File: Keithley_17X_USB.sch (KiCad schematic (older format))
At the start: 17 parts

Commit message: added more stuff!
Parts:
- removed U?: TLP281-4, Package_SO:SOIC-16_4.55x10.3mm_P1.27mm, symbol Isolator:TLP291-4
- added C?: 100nF, symbol Device:C
- added C? (x3): 1uF, symbol Device:C
- added RN? (x2): 10k, symbol Device:R_Pack04
- added U? (x2): TLP281-4, Package_SO:SOIC-16_4.55x10.3mm_P1.27mm, symbol TLP291-4:TLP281-4
- added U?: TPS782, symbol TPS782:TPS782
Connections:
- net labels added: +3V3, B1, B1_IN, B2, B2_IN, B4, B4_IN, B8, B8_IN, CLK, CLK_IN, D5, D5_IN, GNDA, OVERRANGE, OVERRANGE_IN, READING, SBWTCK, SBWTDIO, SIGN, SIGN_IN
- wire segments 62 -> 174
- no-connect marks 5 -> 6
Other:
- moved on the sheet: C?, D?, FB?, J?, R?, U?

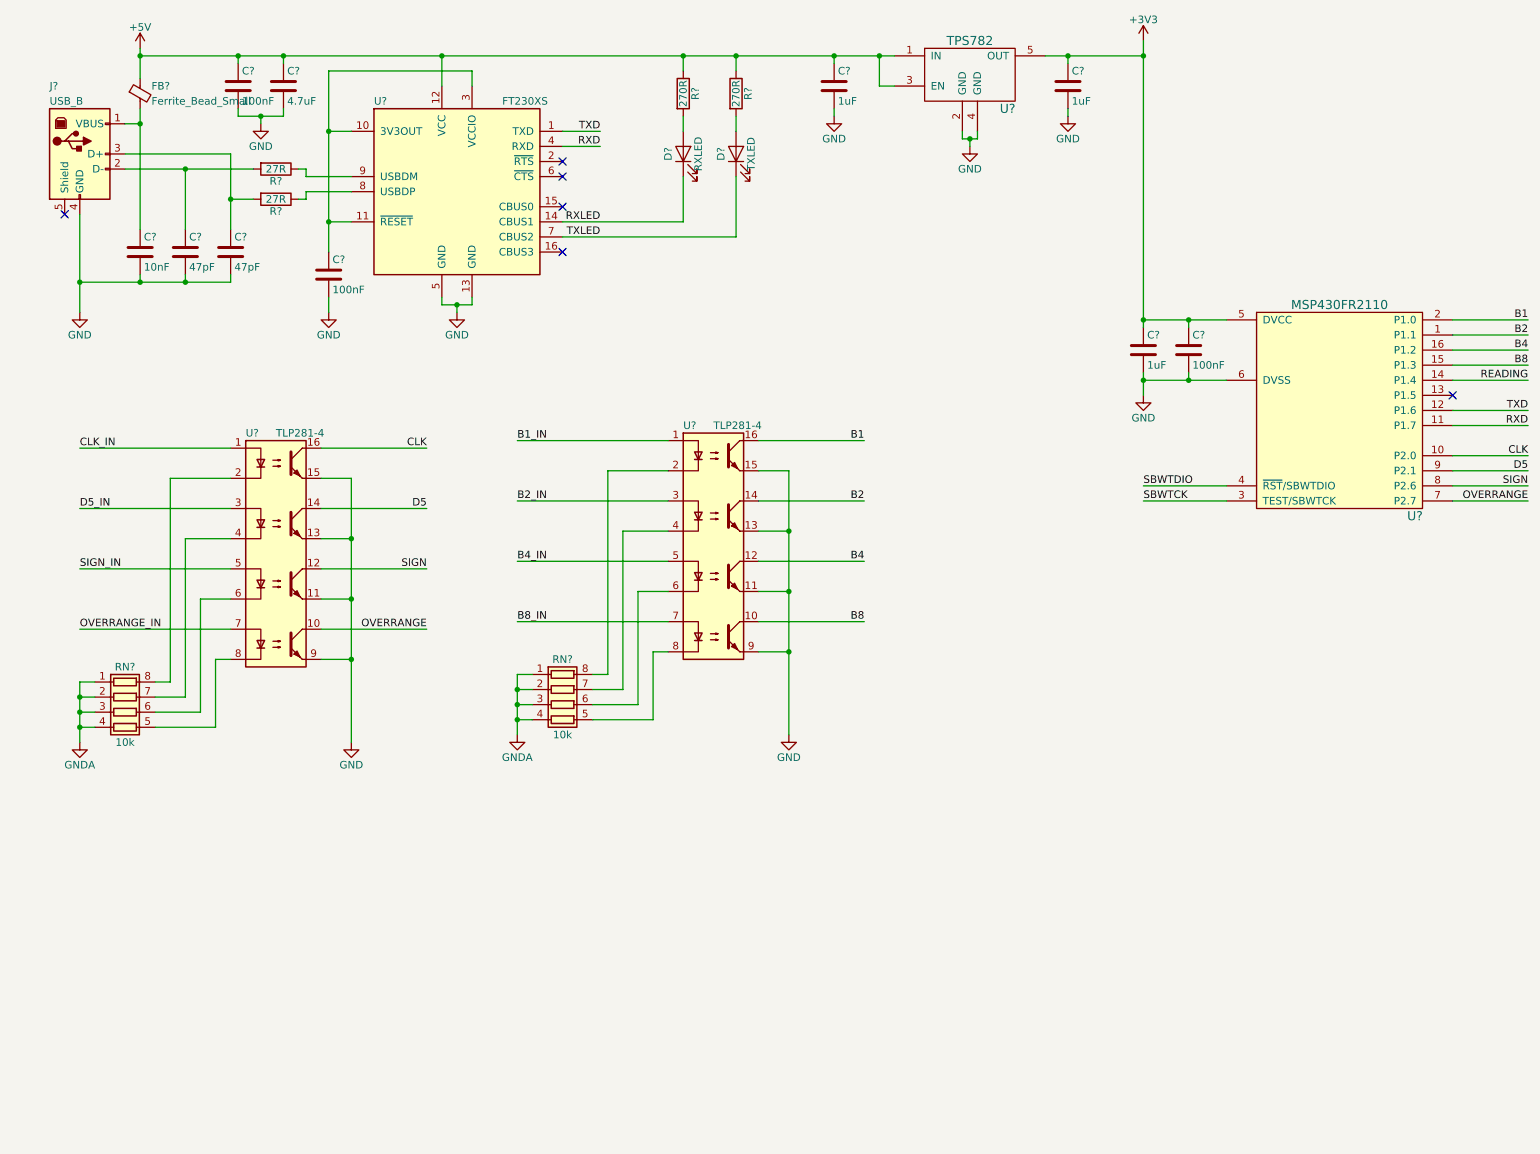
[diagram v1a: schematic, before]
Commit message: clean up schematic, final or darn close
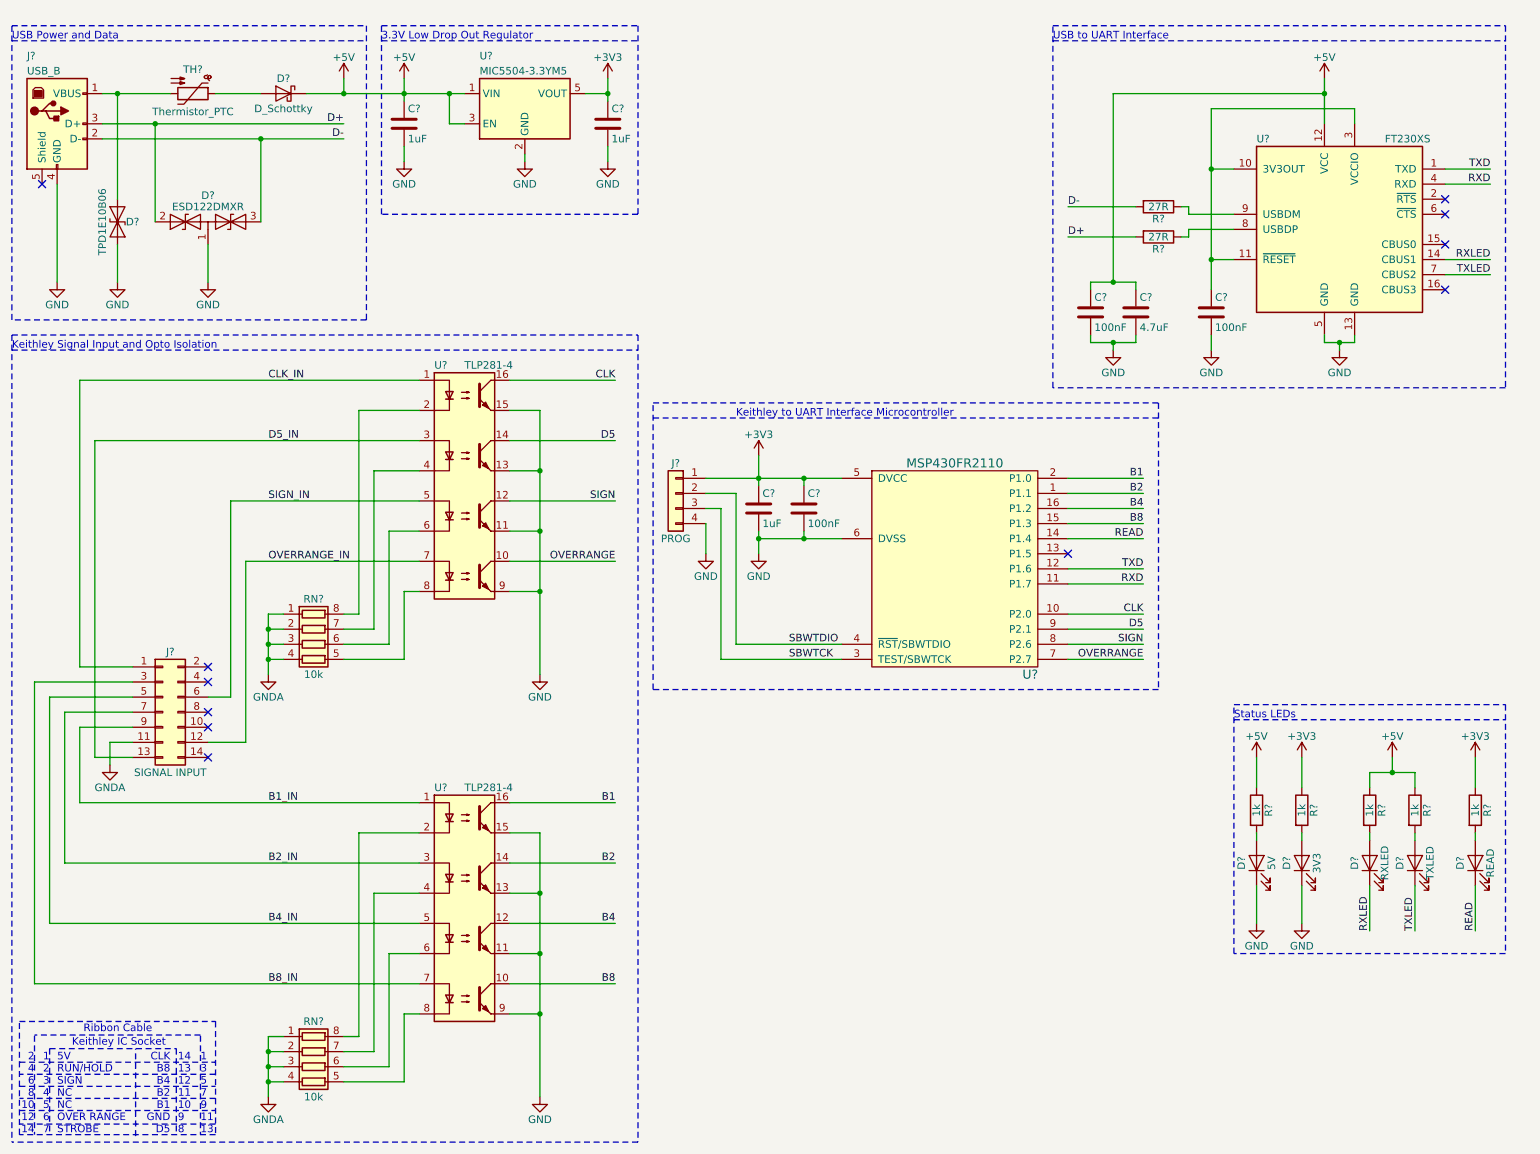
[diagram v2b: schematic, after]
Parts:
- removed C?: 10nF, symbol Device:C
- removed C? (x2): 47pF, symbol Device:C
- removed FB?: Ferrite_Bead_Small, symbol Device:Ferrite_Bead_Small
- removed U?: TPS782, symbol TPS782:TPS782
- added D?: TPD1E10B06, symbol Device:D_TVS
- added D?: ESD122DMXR, symbol Device:D_TVS_x2_CAA
- added D?: D_Schottky, symbol Device:D_Schottky
- added D?: READ, symbol Device:LED
- added D?: 5V, symbol Device:LED
- added D?: 3V3, symbol Device:LED
- added J?: SIGNAL INPUT, symbol Connector_Generic:Conn_02x07_Odd_Even
- added J?: PROG, symbol Connector_Generic:Conn_01x04
- added R? (x3): 1k, symbol Device:R
- added TH?: Thermistor_PTC, symbol Device:Thermistor_PTC
- added U?: MIC5504-3.3YM5, Package_TO_SOT_SMD:SOT-23-5, symbol Regulator_Linear:MIC5504-3.3YM5
- R? (x2): value 270R -> 1k
- U?: Description (none) -> IC MCU 16BIT 2KB FRAM 16TSSOP; Manufacture (none) -> Texas Instruments; Mfg Part Number (none) -> MSP430FR2110IPW16R; Supplier (none) -> Digi-Key; Supplier Part Number (none) -> 296-47343-1-ND
- U?: Description (none) -> IC USB SERIAL BASIC UART 16SSOP; Manufacture (none) -> FTDI, Future Technology Devices International Ltd; Mfg Part Number (none) -> FT230XS-R; Supplier (none) -> Digi-Key; Supplier Part Number (none) -> 768-1135-1-ND
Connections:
- net +3V3: now also J?.1 (Pin_1), R?.1, R?.1, U?.5 (VOUT)
- net +5V: now also D?.1 (K), R?.1, U?.1 (VIN), U?.3 (EN)
- net B1_IN: now also J?.9 (Pin_9)
- net B2_IN: now also J?.7 (Pin_7)
- net B4_IN: now also J?.5 (Pin_5)
- net B8_IN: now also J?.3 (Pin_3)
- net CLK_IN: now also J?.1 (Pin_1)
- net D5_IN: now also J?.13 (Pin_13)
- net GND: now also D?.1 (K), D?.1 (K), D?.1 (common), D?.2 (A2), J?.4 (Pin_4), U?.2 (GND)
- net GNDA: now also J?.11 (Pin_11)
- net OVERRANGE_IN: now also J?.12 (Pin_12)
- net SBWTCK: now also J?.3 (Pin_3)
- net SBWTDIO: now also J?.2 (Pin_2)
- net SIGN_IN: now also J?.6 (Pin_6)
- net at J?.1 (VBUS): now also D?.1 (A1), TH?.2
- net D-: now reaches J?.2 (D-), R?.2
- net D-: now also D?.3 (A2)
- net D+: now reaches J?.3 (D+), R?.2
- net D+: now also D?.2 (A1)
- net READING renamed READ
- net READ: now also D?.1 (K)
- new net: D?.2 (A), TH?.1
- new net: D?.2 (A), R?.2 (x3)
- no-connect marks 6 -> 11
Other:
- note added: "14\n13\n12\n11\n10\n9\n8"
- note added: "1\n2\n3\n4\n5\n6\n7"
- note added: "1\n3\n5\n7\n9\n11\n13"
- note added: "2\n4\n6\n8\n10\n12\n14"
- note added: "3.3V Low Drop Out Regulator"
- note added: "5V\nRUN/HOLD\nSIGN\nNC\nNC\nOVER RANGE\nSTROBE"
- note added: "CLK\nB8\nB4\nB2\nB1\nGND\nD5"
- note added: "Keithley IC Socket"
- note added: "Keithley Signal Input and Opto Isolation"
- note added: "Keithley to UART Interface Microcontroller"
- note added: "Ribbon Cable"
- note added: "Status LEDs"
- note added: "USB Power and Data"
- note added: "USB to UART Interface"
- moved on the sheet: C?, D?, J?, R?, RN?, U?

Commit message: add component feild values
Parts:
- removed RN?: 10k, symbol Device:R_Pack04
- added RN?: 10k, symbol Device:R_Pack04
- C? (x3): Description (none) -> CAP CER 0.1UF 25V Y5V 0603; Manufacture (none) -> KEMET; Mfg Part Number (none) -> C0603C104Z3VACTU; Supplier (none) -> Digi-Key; Supplier Part Number (none) -> 399-1100-1-ND
- C?: Description (none) -> CAP CER 4.7UF 6.3V X5R 0603; Manufacture (none) -> Samsung Electro-Mechanics; Mfg Part Number (none) -> CL10A475KQ8NNNC; Supplier (none) -> Digi-Key; Supplier Part Number (none) -> 1276-1045-1-ND
- C? (x3): Description (none) -> CAP CER 1UF 6.3V X5R 0603; Manufacture (none) -> Samsung Electro-Mechanics; Mfg Part Number (none) -> CL10A105KQ8NNNC; Supplier (none) -> Digi-Key; Supplier Part Number (none) -> 1276-1036-1-ND
- D?: Description (none) -> SCHOTTKY 60V SOD-123FL; Manufacture (none) -> SMC Diode Solutions; Mfg Part Number (none) -> DSS16UTR; Supplier (none) -> Digi-Key; Supplier Part Number (none) -> 1655-1929-1-ND
- J?: Description (none) -> CONN RCPT TYPEB 4POS R/A; Manufacture (none) -> Pulse Electronics Network; Mfg Part Number (none) -> E8144-B02022-L; Supplier (none) -> Digi-Key; Supplier Part Number (none) -> 553-2272-ND
- R? (x2): Description (none) -> RES 27 OHM 5% 1/10W 0603; Manufacture (none) -> Stackpole Electronics Inc; Mfg Part Number (none) -> RMCF0603JT27R0; Supplier (none) -> Digi-Key; Supplier Part Number (none) -> RMCF0603JT27R0CT-ND
- R? (x5): Description (none) -> RES SMD 1K OHM 5% 1/10W 0603; Manufacture (none) -> Yageo; Mfg Part Number (none) -> RC0603JR-071KL; Supplier (none) -> Digi-Key; Supplier Part Number (none) -> 311-1.0KGRCT-ND
- RN?: Description (none) -> RES ARRAY 4 RES 10K OHM 2012; Manufacture (none) -> Yageo; Mfg Part Number (none) -> YC324-JK-0710KL; Supplier (none) -> Digi-Key; Supplier Part Number (none) -> YC324J-10KCT-ND
- TH?: Description (none) -> PTC RESET FUSE 8V 500MA 1206; Manufacture (none) -> Bel Fuse Inc.; Mfg Part Number (none) -> 0ZCJ0050FF2G; Supplier (none) -> Digi-Key; Supplier Part Number (none) -> 507-1802-1-ND
- U? (x2): Description (none) -> OPTOISO 2.5KV 4CH TRANS 16-SOP; Manufacture (none) -> Toshiba Semiconductor and Storage; Mfg Part Number (none) -> TLP281-4(GB-TP,J,F
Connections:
- net GNDA: now also RN?.1 (R1.1), RN?.2 (R2.1), RN?.3 (R3.1), RN?.4 (R4.1)
- net at U?.8: now also RN?.5 (R4.2)
- net at U?.6: now also RN?.6 (R3.2)
- net at U?.4: now also RN?.7 (R2.2)
- net at U?.2: now also RN?.8 (R1.2)

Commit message: annotate
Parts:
- added H1, H2, H3, H4: CaseMnt, symbol Mechanical:MountingHole_Pad
- gave numbers to parts that had none: 33
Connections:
- net GND: now also H1.1, H2.1, H3.1, H4.1

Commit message: update with footprints
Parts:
- C1, C2, C3, C4, C5, C6, C7: footprint (none) -> Capacitor_SMD:C_0603_1608Metric
- D2: footprint (none) -> TI_TVSDiode:TI_DMX_X2SON
- D4, D5, D6, D7, D8: footprint (none) -> LED_SMD:LED_0805_2012Metric
- J1: footprint (none) -> Connector_USB:USB_B_OST_USB-B1HSxx_Horizontal
- R1, R2, R3, R4, R5, R6, R7: footprint (none) -> Resistor_SMD:R_0603_1608Metric
- TH1: footprint (none) -> Fuse:Fuse_1206_3216Metric
- U4: footprint (none) -> Package_SO:TSSOP-16_4.4x5mm_P0.65mm
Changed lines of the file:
@@
 F 0 "U4" H 7300 2250 60  0000 C CNN
 F 1 "MSP430FR2110" H 6800 3650 60  0000 C CNN
-F 2 "" H 7100 3000 60  0001 C CNN
+F 2 "Package_SO:TSSOP-16_4.4x5mm_P0.65mm" H 7100 3000 60  0001 C CNN
 F 3 "http://www.ti.com/lit/ds/symlink/msp430fr2111.pdf" H 7100 3000 60  0001 C CNN
 F 4 "IC MCU 16BIT 2KB FRAM 16TSSOP" H 6800 3550 50  0001 C CNN "Description"
@@
 F 0 "J1" H 650 1650 50  0000 L CNN
 F 1 "USB_B" H 650 1550 50  0000 L CNN
-F 2 "" H 1000 1150 50  0001 C CNN
+F 2 "Connector_USB:USB_B_OST_USB-B1HSxx_Horizontal" H 1000 1150 50  0001 C CNN
 F 3 "https://productfinder.pulseeng.com/doc_type/WEB301/doc_num/E8144-B02022-L/doc_part/E8144-B02022-L.pdf" H 1000 1150 50  0001 C CNN
 F 4 "CONN RCPT TYPEB 4POS R/A" H 850 1200 50  0001 C CNN "Description"
@@
 F 0 "R1" V 8230 1750 50  0000 C CNN
 F 1 "27R" V 8150 1750 50  0000 C CNN
-F 2 "" V 8080 1750 50  0001 C CNN
+F 2 "Resistor_SMD:R_0603_1608Metric" V 8080 1750 50  0001 C CNN
 F 3 "https://www.seielect.com/Catalog/SEI-RMCF_RMCP.pdf" H 8150 1750 50  0001 C CNN
 F 4 "RES 27 OHM 5% 1/10W 0603" H 0   0   50  0001 C CNN "Description"
@@
 F 0 "R2" V 8230 1950 50  0000 C CNN
 F 1 "27R" V 8150 1950 50  0000 C CNN
-F 2 "" V 8080 1950 50  0001 C CNN
+F 2 "Resistor_SMD:R_0603_1608Metric" V 8080 1950 50  0001 C CNN
 F 3 "https://www.seielect.com/Catalog/SEI-RMCF_RMCP.pdf" H 8150 1950 50  0001 C CNN
 F 4 "RES 27 OHM 5% 1/10W 0603" H 0   0   50  0001 C CNN "Description"
@@
 F 0 "C7" H 8525 2550 50  0000 L CNN
 F 1 "100nF" H 8525 2350 50  0000 L CNN
-F 2 "" H 8538 2300 50  0001 C CNN
+F 2 "Capacitor_SMD:C_0603_1608Metric" H 8538 2300 50  0001 C CNN
 F 3 "https://api.kemet.com/component-edge/download/datasheet/C0603C104Z3VACTU.pdf" H 8500 2450 50  0001 C CNN
 F 4 "CAP CER 0.1UF 25V Y5V 0603" H 0   0   50  0001 C CNN "Description"
@@
 F 0 "C6" H 8025 2550 50  0000 L CNN
 F 1 "4.7uF" H 8025 2350 50  0000 L CNN
-F 2 "" H 8038 2300 50  0001 C CNN
+F 2 "Capacitor_SMD:C_0603_1608Metric" H 8038 2300 50  0001 C CNN
 F 3 "http://www.samsungsem.com/kr/support/product-search/mlcc/CL10A475KQ8NNNC.jsp" H 8000 2450 50  0001 C CNN
 F 4 "CAP CER 4.7UF 6.3V X5R 0603" H 8000 2450 50  0001 C CNN "Description"
@@
 F 0 "C5" H 7725 2550 50  0000 L CNN
 F 1 "100nF" H 7725 2350 50  0000 L CNN
-F 2 "" H 7738 2300 50  0001 C CNN
+F 2 "Capacitor_SMD:C_0603_1608Metric" H 7738 2300 50  0001 C CNN
 F 3 "https://api.kemet.com/component-edge/download/datasheet/C0603C104Z3VACTU.pdf" H 7700 2450 50  0001 C CNN
 F 4 "CAP CER 0.1UF 25V Y5V 0603" H 0   0   50  0001 C CNN "Description"
@@
 F 0 "D6" H 9550 6200 50  0000 C CNN
 F 1 "RXLED" H 9550 6000 50  0000 C CNN
-F 2 "" H 9550 6100 50  0001 C CNN
+F 2 "LED_SMD:LED_0805_2012Metric" H 9550 6100 50  0001 C CNN
 F 3 "~" H 9550 6100 50  0001 C CNN
 	1    9550 6100
@@
 F 0 "D7" H 9850 6200 50  0000 C CNN
 F 1 "TXLED" H 9850 6000 50  0000 C CNN
-F 2 "" H 9850 6100 50  0001 C CNN
+F 2 "LED_SMD:LED_0805_2012Metric" H 9850 6100 50  0001 C CNN
 F 3 "~" H 9850 6100 50  0001 C CNN
 	1    9850 6100
@@
 F 0 "R5" V 9630 5750 50  0000 C CNN
 F 1 "1k" V 9550 5750 50  0000 C CNN
-F 2 "" V 9480 5750 50  0001 C CNN
+F 2 "Resistor_SMD:R_0603_1608Metric" V 9480 5750 50  0001 C CNN
 F 3 "http://www.yageo.com/documents/recent/PYu-RC_Group_51_RoHS_L_10.pdf" H 9550 5750 50  0001 C CNN
 F 4 "RES SMD 1K OHM 5% 1/10W 0603" H 0   0   50  0001 C CNN "Description"
@@
 F 0 "R6" V 9930 5750 50  0000 C CNN
 F 1 "1k" V 9850 5750 50  0000 C CNN
-F 2 "" V 9780 5750 50  0001 C CNN
+F 2 "Resistor_SMD:R_0603_1608Metric" V 9780 5750 50  0001 C CNN
 F 3 "http://www.yageo.com/documents/recent/PYu-RC_Group_51_RoHS_L_10.pdf" H 9850 5750 50  0001 C CNN
 F 4 "RES SMD 1K OHM 5% 1/10W 0603" H 0   0   50  0001 C CNN "Description"
@@
 F 0 "C4" H 5825 3850 50  0000 L CNN
 F 1 "100nF" H 5825 3650 50  0000 L CNN
-F 2 "" H 5838 3600 50  0001 C CNN
+F 2 "Capacitor_SMD:C_0603_1608Metric" H 5838 3600 50  0001 C CNN
 F 3 "https://api.kemet.com/component-edge/download/datasheet/C0603C104Z3VACTU.pdf" H 5800 3750 50  0001 C CNN
 F 4 "CAP CER 0.1UF 25V Y5V 0603" H 0   0   50  0001 C CNN "Description"
@@
 F 0 "C3" H 5525 3850 50  0000 L CNN
 F 1 "1uF" H 5525 3650 50  0000 L CNN
-F 2 "" H 5538 3600 50  0001 C CNN
+F 2 "Capacitor_SMD:C_0603_1608Metric" H 5538 3600 50  0001 C CNN
 F 3 "http://www.samsungsem.com/kr/support/product-search/mlcc/CL10A105KQ8NNNC.jsp" H 5500 3750 50  0001 C CNN
 F 4 "CAP CER 1UF 6.3V X5R 0603" H 0   0   50  0001 C CNN "Description"
@@
 F 0 "C1" H 3175 1300 50  0000 L CNN
 F 1 "1uF" H 3175 1100 50  0000 L CNN
-F 2 "" H 3188 1050 50  0001 C CNN
+F 2 "Capacitor_SMD:C_0603_1608Metric" H 3188 1050 50  0001 C CNN
 F 3 "http://www.samsungsem.com/kr/support/product-search/mlcc/CL10A105KQ8NNNC.jsp" H 3150 1200 50  0001 C CNN
 F 4 "CAP CER 1UF 6.3V X5R 0603" H 0   0   50  0001 C CNN "Description"
@@
 F 0 "C2" H 4525 1300 50  0000 L CNN
 F 1 "1uF" H 4525 1100 50  0000 L CNN
-F 2 "" H 4538 1050 50  0001 C CNN
+F 2 "Capacitor_SMD:C_0603_1608Metric" H 4538 1050 50  0001 C CNN
 F 3 "http://www.samsungsem.com/kr/support/product-search/mlcc/CL10A105KQ8NNNC.jsp" H 4500 1200 50  0001 C CNN
 F 4 "CAP CER 1UF 6.3V X5R 0603" H 0   0   50  0001 C CNN "Description"
@@
 F 0 "TH1" V 1590 1000 50  0000 C CNN
 F 1 "Thermistor_PTC" V 1870 1000 50  0000 C CNN
-F 2 "" H 1800 800 50  0001 L CNN
+F 2 "Fuse:Fuse_1206_3216Metric" H 1800 800 50  0001 L CNN
 F 3 "https://www.belfuse.com/resources/CircuitProtection/datasheets/0ZCJ%20Nov2016.pdf" H 1750 1000 50  0001 C CNN
 F 4 "PTC RESET FUSE 8V 500MA 1206" H 1750 1000 50  0001 C CNN "Description"
@@
 F 0 "D2" H 1850 2025 50  0000 C CNN
 F 1 "ESD122DMXR" H 1850 1950 50  0000 C CNN
-F 2 "" H 1700 1850 50  0001 C CNN
+F 2 "TI_TVSDiode:TI_DMX_X2SON" H 1700 1850 50  0001 C CNN
 F 3 "http://www.ti.com/lit/ds/symlink/esd122.pdf" H 1700 1850 50  0001 C CNN
 F 4 "TVS DIODE 8.4VC 2.5A IPP 3X2SON" H 1850 1850 50  0001 C CNN "Description"
@@
 F 0 "D8" H 10250 6200 50  0000 C CNN
 F 1 "READ" H 10250 6000 50  0000 C CNN
-F 2 "" H 10250 6100 50  0001 C CNN
+F 2 "LED_SMD:LED_0805_2012Metric" H 10250 6100 50  0001 C CNN
 F 3 "~" H 10250 6100 50  0001 C CNN
 	1    10250 6100
@@
 F 0 "R7" V 10330 5750 50  0000 C CNN
 F 1 "1k" V 10250 5750 50  0000 C CNN
-F 2 "" V 10180 5750 50  0001 C CNN
+F 2 "Resistor_SMD:R_0603_1608Metric" V 10180 5750 50  0001 C CNN
 F 3 "http://www.yageo.com/documents/recent/PYu-RC_Group_51_RoHS_L_10.pdf" H 10250 5750 50  0001 C CNN
 F 4 "RES SMD 1K OHM 5% 1/10W 0603" H 0   0   50  0001 C CNN "Description"
@@
 F 0 "D4" H 8800 6200 50  0000 C CNN
 F 1 "5V" H 8800 6000 50  0000 C CNN
-F 2 "" H 8800 6100 50  0001 C CNN
+F 2 "LED_SMD:LED_0805_2012Metric" H 8800 6100 50  0001 C CNN
 F 3 "~" H 8800 6100 50  0001 C CNN
 	1    8800 6100
@@
 F 0 "D5" H 9100 6200 50  0000 C CNN
 F 1 "3V3" H 9100 6000 50  0000 C CNN
-F 2 "" H 9100 6100 50  0001 C CNN
+F 2 "LED_SMD:LED_0805_2012Metric" H 9100 6100 50  0001 C CNN
 F 3 "~" H 9100 6100 50  0001 C CNN
 	1    9100 6100
@@
 F 0 "R4" V 9180 5750 50  0000 C CNN
 F 1 "1k" V 9100 5750 50  0000 C CNN
-F 2 "" V 9030 5750 50  0001 C CNN
+F 2 "Resistor_SMD:R_0603_1608Metric" V 9030 5750 50  0001 C CNN
 F 3 "http://www.yageo.com/documents/recent/PYu-RC_Group_51_RoHS_L_10.pdf" H 9100 5750 50  0001 C CNN
 F 4 "RES SMD 1K OHM 5% 1/10W 0603" H 0   0   50  0001 C CNN "Description"
@@
 F 0 "R3" V 8880 5750 50  0000 C CNN
 F 1 "1k" V 8800 5750 50  0000 C CNN
-F 2 "" V 8730 5750 50  0001 C CNN
+F 2 "Resistor_SMD:R_0603_1608Metric" V 8730 5750 50  0001 C CNN
 F 3 "http://www.yageo.com/documents/recent/PYu-RC_Group_51_RoHS_L_10.pdf" H 8800 5750 50  0001 C CNN
 F 4 "RES SMD 1K OHM 5% 1/10W 0603" H 0   0   50  0001 C CNN "Description"
